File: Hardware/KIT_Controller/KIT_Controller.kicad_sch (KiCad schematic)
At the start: 11 parts, among them U101 Nokia_5110_LCD

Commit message: Fixup drc
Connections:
- no-connect marks 5 -> 10
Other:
- sheet MCU ports: added MISO, MOSI, SCK, SCL, SDA; removed none
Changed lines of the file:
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@@
   )
   (no_connect (at 212.09 97.155))
+  (no_connect (at 53.34 46.99))
+  (no_connect (at 53.34 54.61))
   (no_connect (at 212.09 92.075))
   (no_connect (at 212.09 94.615))
   (no_connect (at 212.09 88.265))
+  (no_connect (at 53.34 52.705))
   (no_connect (at 212.09 99.695))
+  (no_connect (at 53.34 45.085))
+  (no_connect (at 53.34 48.895))
   (wire (pts (xy 221.615 76.2) (xy 226.06 76.2))
     (stroke (width 0) (type default) (color 0 0 0 0))
@@
     (stroke (width 0) (type default) (color 0 0 0 0))
   )
+  (wire (pts (xy 47.625 52.705) (xy 53.34 52.705))
+    (stroke (width 0) (type default) (color 0 0 0 0))
+  )
   (wire (pts (xy 210.82 76.2) (xy 213.995 76.2))
     (stroke (width 0) (type default) (color 0 0 0 0))
@@
     (stroke (width 0) (type default) (color 0 0 0 0))
   )
+  (wire (pts (xy 47.625 46.99) (xy 53.34 46.99))
+    (stroke (width 0) (type default) (color 0 0 0 0))
+  )
   (wire (pts (xy 226.06 76.2) (xy 226.06 76.835))
     (stroke (width 0) (type default) (color 0 0 0 0))
@@
     (stroke (width 0) (type default) (color 0 0 0 0))
   )
+  (wire (pts (xy 47.625 54.61) (xy 53.34 54.61))
+    (stroke (width 0) (type default) (color 0 0 0 0))
+  )
   (wire (pts (xy 255.905 95.25) (xy 255.905 97.155))
     (stroke (width 0) (type default) (color 0 0 0 0))
@@
     (stroke (width 0) (type default) (color 0 0 0 0))
   )
+  (wire (pts (xy 47.625 48.895) (xy 53.34 48.895))
+    (stroke (width 0) (type default) (color 0 0 0 0))
+  )
   (wire (pts (xy 227.33 111.76) (xy 227.33 114.3))
     (stroke (width 0) (type default) (color 0 0 0 0))
@@
   )
   (wire (pts (xy 227.33 107.315) (xy 227.33 111.76))
+    (stroke (width 0) (type default) (color 0 0 0 0))
+  )
+  (wire (pts (xy 47.625 45.085) (xy 53.34 45.085))
     (stroke (width 0) (type default) (color 0 0 0 0))
   )
@@
     (pin "2")
   )
-  (sheet (at 26.67 40.64) (size 51.435 28.575) (fields_autoplaced)
+  (sheet (at 26.67 40.64) (size 20.955 37.465) (fields_autoplaced)
     (stroke (width 0.1524) (type solid) (color 0 0 0 0))
     (fill (color 0 0 0 0.0000))
@@
       (effects (font (size 1.27 1.27)) (justify left bottom))
     )
-    (property "Sheet file" "mcu.kicad_sch" (id 1) (at 26.67 69.7996 0)
+    (property "Sheet file" "mcu.kicad_sch" (id 1) (at 26.67 78.6896 0)
       (effects (font (size 1.27 1.27)) (justify left top))
     )
-  )
+    (pin "MOSI" output (at 47.625 46.99 0)
+      (effects (font (size 1.27 1.27)) (justify right))
+    )
+    (pin "SCK" output (at 47.625 48.895 0)
+      (effects (font (size 1.27 1.27)) (justify right))
+    )
+    (pin "MISO" input (at 47.625 45.085 0)
+      (effects (font (size 1.27 1.27)) (justify right))
+    )
+    (pin "SDA" bidirectional (at 47.625 52.705 0)
+      (effects (font (size 1.27 1.27)) (justify right))
+    )
+    (pin "SCL" output (at 47.625 54.61 0)
+      (effects (font (size 1.27 1.27)) (justify right))
+    )
+  )

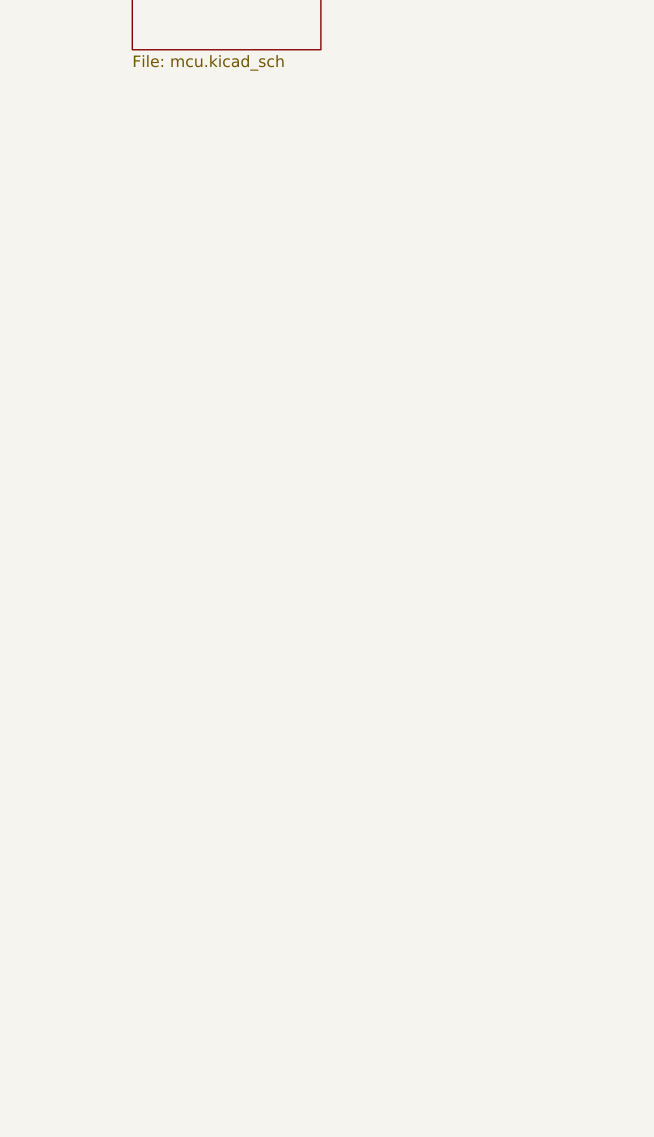
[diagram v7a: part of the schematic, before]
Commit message: Add short range modem
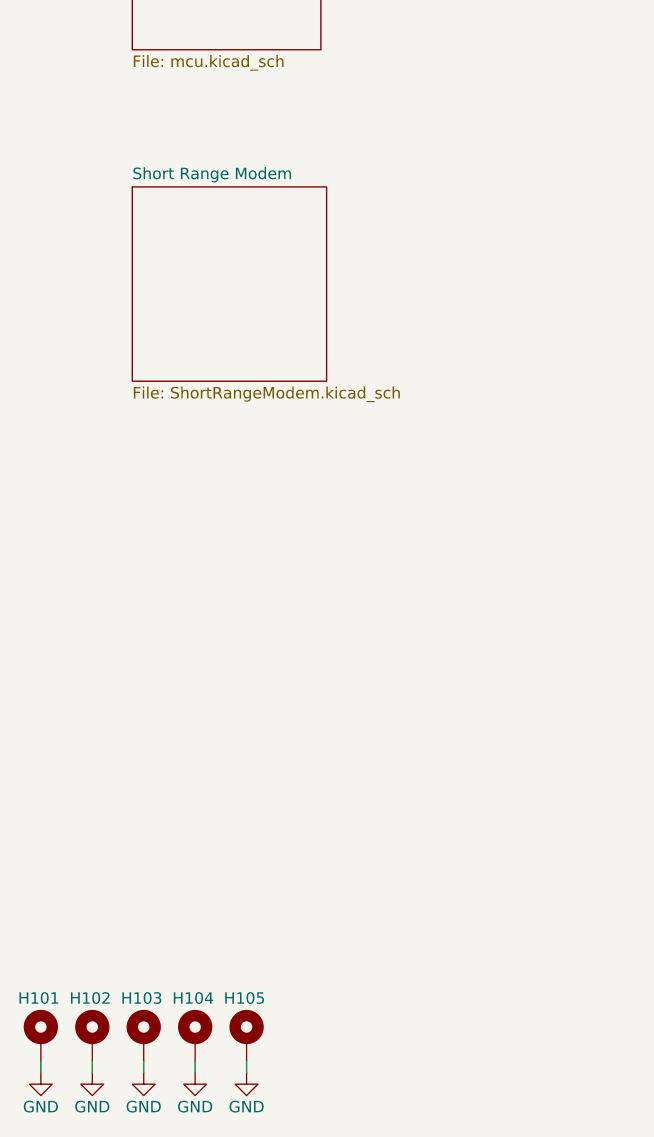
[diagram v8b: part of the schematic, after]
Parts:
- added H101, H102, H103, H104, H105: MountingHole_Pad, MountingHole:MountingHole_2.5mm_Pad_TopBottom, symbol Mechanical:MountingHole_Pad
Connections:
- net GND: now also H101.1, H102.1, H103.1, H104.1, H105.1
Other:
- added sheet Short Range Modem (ShortRangeModem.kicad_sch)
